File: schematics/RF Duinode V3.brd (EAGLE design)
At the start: 50.2 x 28.6 mm, 24 parts, among them IC2 ATMEGA328, IC3 MCP9700, Q1 8MHz

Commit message: fixed previous commit
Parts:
- removed G2: CR2450H, JC:122-00224-GR
- JP6: value EXTPWR -> BATT
- moved R2 8.50 mm to (18.5, 26.0)
- moved R3 8.00 mm to (10.5, 26.0)
- moved LED1 0.50 mm to (14.5, 26.0), turned to 0 degrees
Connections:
- net EXTPWR renamed BATT
- removed net COIN: G2.+, SW_PWR.3
- new net EXT_VSUPPLY: JP7.VCC, SW_PWR.3
- net +3V3: no longer JP7.VCC
- net GND: no longer G2.-
- net GRN_LED: now also R3.2
- net RED_LED: now also R2.1
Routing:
- net EXT_VSUPPLY: track 0.00 -> 40.3 mm, vias 0 -> 2
- net GND: track 156.5 -> 117.3 mm, vias 4 -> 2
- net COIN: track 39.0 -> 0.00 mm, vias 1 -> 0
- net RED_LED: track 0.00 -> 15.7 mm
- net N$2: track 14.7 -> 0.00 mm
- net +3V3: track 111.8 -> 123.8 mm
- net N$4: track 1.71 -> 0.00 mm
- net GRN_LED: track 35.8 -> 37.3 mm
- net N$1: track 2.69 -> 1.94 mm
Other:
- board text added: "BATT/EXT"
- board text added: "GND"
- board text added: "RF24 Node V1"
- board text removed: "BLK"
- board text removed: "COIN/EXT"
- board text removed: "GRN"
- board text removed: "RF Duinode V3 (2V4)"

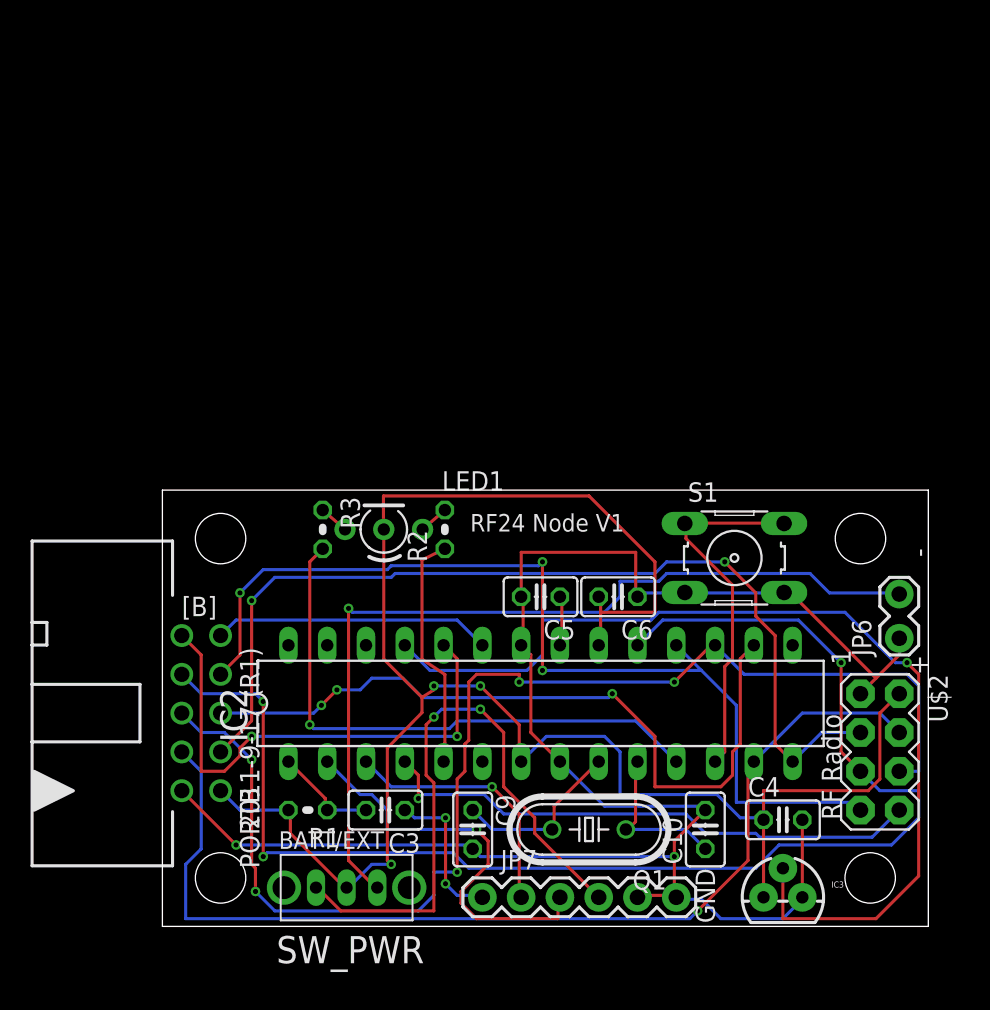
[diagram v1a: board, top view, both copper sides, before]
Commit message: Rotated board by 90deg
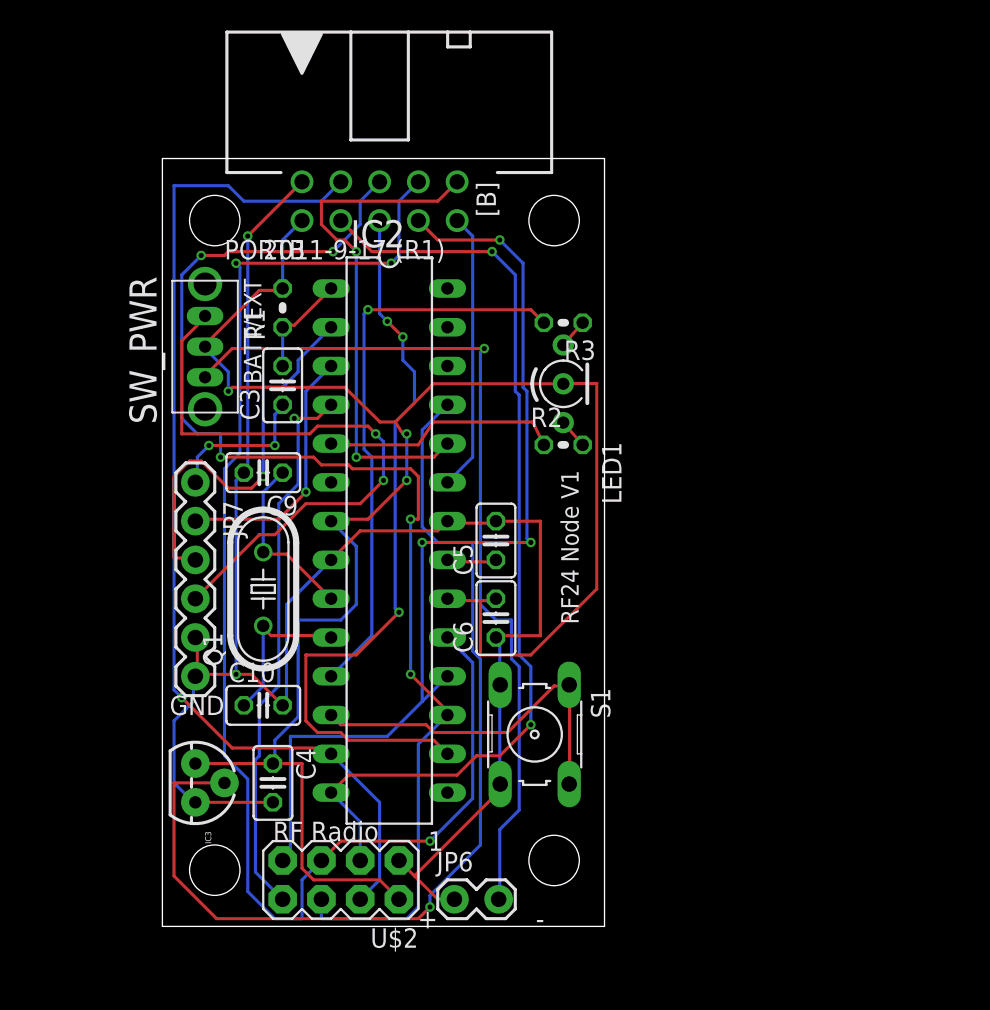
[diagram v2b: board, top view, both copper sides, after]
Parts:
- moved JP2 43.1 mm to (3.43, 46.2), turned to 270 degrees
- moved JP9 42.9 mm to (3.43, 3.68), turned to 270 degrees
- moved IC3 39.2 mm to (2.16, 9.40), turned to 270 degrees
- moved SW_PWR 36.6 mm to (2.79, 38.0), turned to 90 degrees
- moved U$2 36.3 mm to (11.7, 3.05), turned to 180 degrees
- moved PORTB 35.5 mm to (14.2, 47.5), turned to 0 degrees
- moved JP6 33.7 mm to (19.3, 1.78), turned to 0 degrees
- moved C4 33.5 mm to (7.24, 9.40), turned to 270 degrees
- moved JP7 33.0 mm to (2.16, 29.1), turned to 270 degrees
- moved R1 32.9 mm to (7.87, 40.5), turned to 90 degrees
- moved JP8 30.2 mm to (25.7, 46.2), turned to 270 degrees
- moved C10 30.1 mm to (6.60, 14.5), turned to 0 degrees
- moved JP1 29.1 mm to (25.7, 4.32), turned to 270 degrees
- moved C3 28.6 mm to (7.87, 35.4), turned to 90 degrees
- moved C9 27.1 mm to (6.60, 29.7), turned to 180 degrees
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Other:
- board size 50.2 x 28.6 mm -> 29 x 50.3 mm

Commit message: Resized and ready for printing
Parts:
- moved PORTB 0.76 mm to (14.2, 46.7)
- moved JP2 0.25 mm to (3.43, 46.0)
- moved JP8 0.25 mm to (25.7, 46.0)
- moved C5 0.25 mm to (21.8, 25.0)
- moved C6 0.25 mm to (21.8, 19.9)
- moved C9 0.25 mm to (6.60, 29.5)
- moved IC2 0.25 mm to (14.9, 25.0)
- moved R2 0.25 mm to (26.3, 31.3)
- moved JP9 0.25 mm to (3.43, 3.43)
- moved C10 0.25 mm to (6.60, 14.2)
- moved C4 0.25 mm to (7.24, 9.14)
- moved IC3 0.25 mm to (2.16, 9.14)
- moved JP1 0.25 mm to (25.7, 4.06)
- moved S1 0.25 mm to (24.4, 12.3)
- moved C3 0.25 mm to (7.87, 35.2)
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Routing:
- net MISO: track 64.3 -> 61.8 mm, vias 3 -> 1
- net UCA1: track 33.8 -> 34.7 mm, vias 2 -> 1
- net SCK: track 90.0 -> 89.0 mm
- net +3V3: track 123.8 -> 123.2 mm
- net RFCE: track 62.9 -> 62.4 mm
- net GND: track 117.3 -> 116.8 mm
- net UC10: track 49.0 -> 48.5 mm
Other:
- board size 29 x 50.3 mm -> 29 x 49 mm
- board text added: "DTR"
- board text added: "RF"
- board text removed: "2011-9-17 (R1)"
- board text removed: "RF Radio"
